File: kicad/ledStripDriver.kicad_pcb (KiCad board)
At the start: 2 copper layers, 110 x 91 mm, 50 parts, among them J1 AudioJack3_SwitchTR, K1 G5RL1AELN5DC, Q1 Q_NPN_BEC_S8050, Q2 AO3400, Q3 AO3400, Q4 AO3400, SW1 SW_DIP_x01, SW2 Rotary_Encoder_Switch, SW3 SW_Push, U1 MOD_ESP32_DEV_universal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

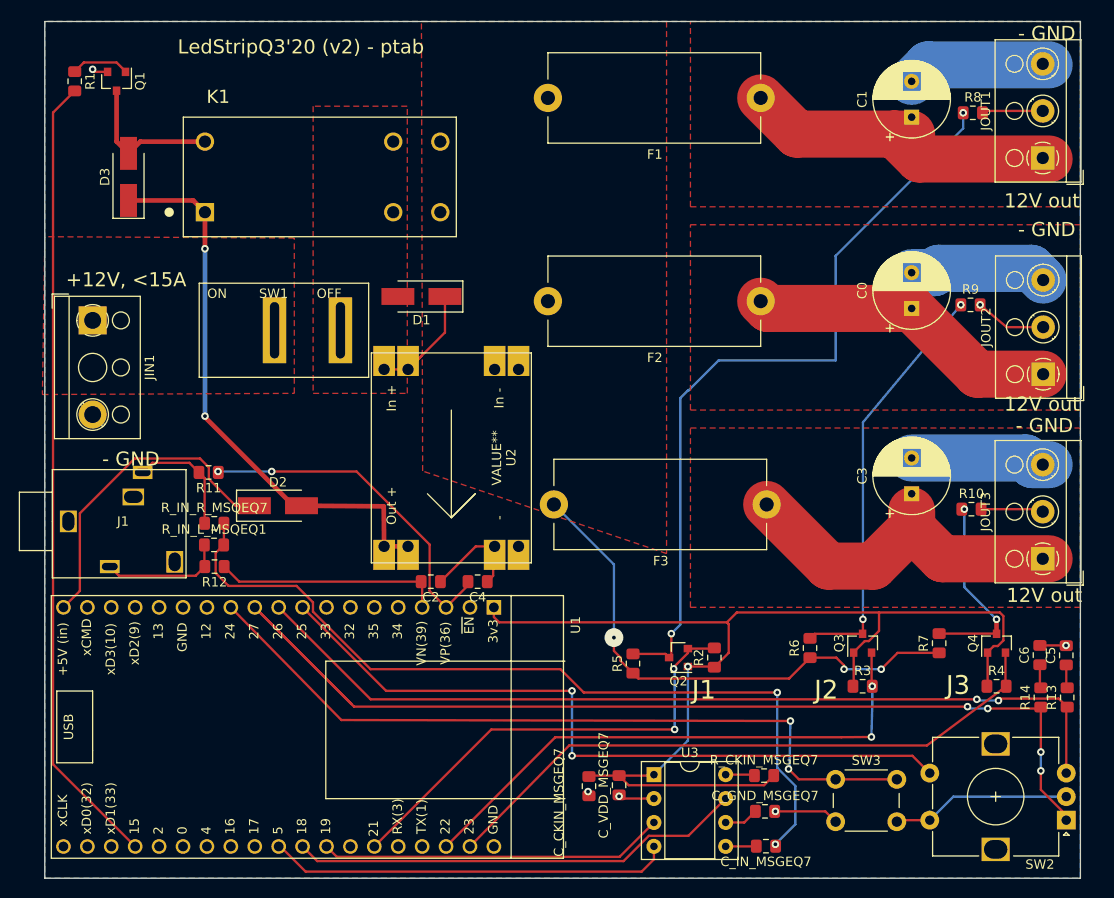
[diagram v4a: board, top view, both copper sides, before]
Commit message: PCB v3: Hopefully manufacturing ready.
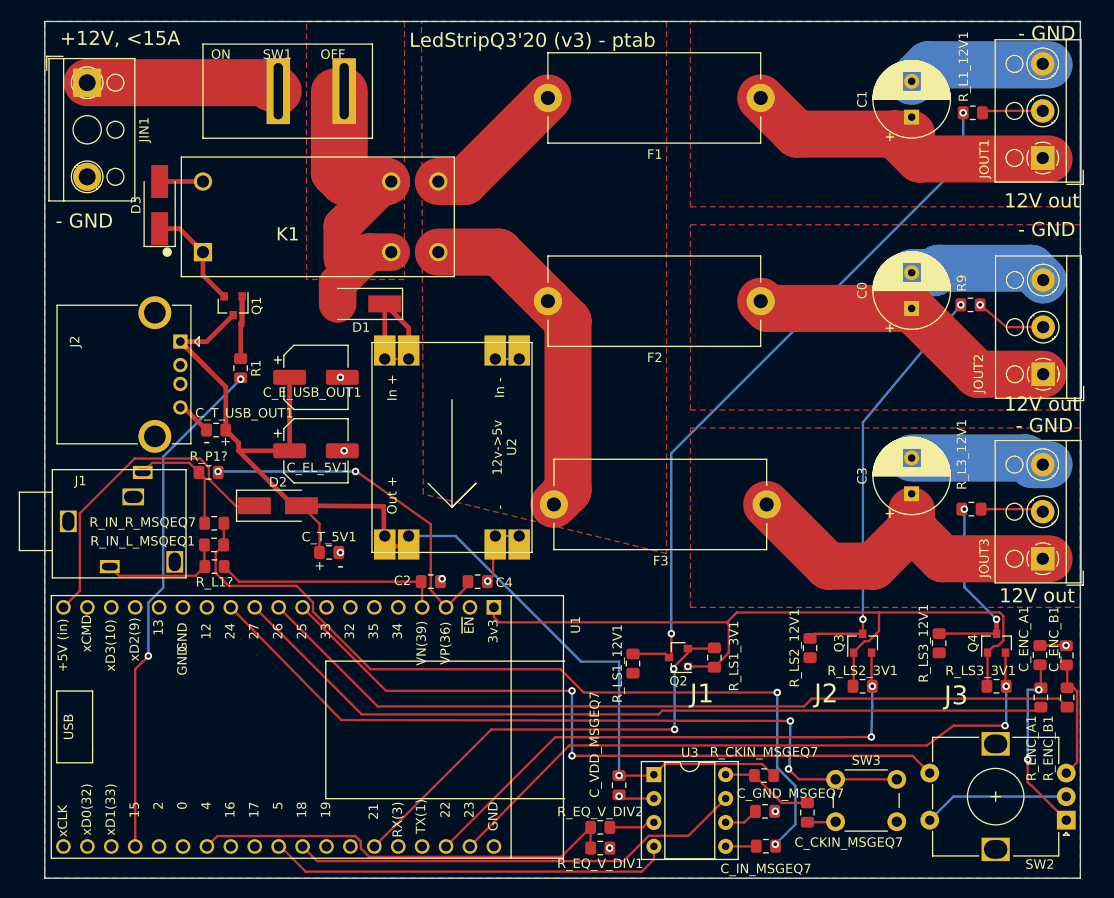
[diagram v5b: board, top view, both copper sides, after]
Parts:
- added C_EL_5V1: >50uF, Capacitor_SMD:CP_Elec_6.3x5.4, F.Cu at (128.8, 95.6)
- added C_E_USB_OUT1: >20uF, Capacitor_SMD:CP_Elec_6.3x5.4, F.Cu at (128.8, 87.8)
- added C_T_5V1: 1uF, Capacitor_SMD:C_0805_2012Metric_Pad1.15x1.40mm_HandSolder, F.Cu at (130.2, 106.4)
- added C_T_USB_OUT1: >1uF, Capacitor_SMD:C_0805_2012Metric_Pad1.15x1.40mm_HandSolder, F.Cu at (118.2, 93.4)
- added J2: USB_POWER_OUT, Connector_USB:USB_A_CONNFLY_DS1095-WNR0, F.Cu at (114.4, 84.0)
- added R_EQ_V_DIV1: 10k, Resistor_SMD:R_0805_2012Metric_Pad1.15x1.40mm_HandSolder, F.Cu at (159.0, 137.8)
- added R_EQ_V_DIV2: 10k, Resistor_SMD:R_0805_2012Metric_Pad1.15x1.40mm_HandSolder, F.Cu at (159.0, 135.6)
- R1: value 47ohm -> ~47ohm
- R9: value 300ohm -> R_L2_12V
- R_L1?: renamed from R12; value R -> xxk?
- R_L1_12V1: renamed from R8; value 300ohm -> 300
- R_L3_12V1: renamed from R10; value 300ohm -> 300
- R_LS1_12V1: renamed from R5; value 5kOhm -> 4k7
- R_LS1_3V1: renamed from R2; value 5kOhm -> 4k7
- R_LS2_12V1: renamed from R6; value 5kOhm -> 4k7
- R_LS2_3V1: renamed from R3; value 5kOhm -> 4k7
- R_LS3_12V1: renamed from R7; value 5kOhm -> 4k7
- R_LS3_3V1: renamed from R4; value 5kOhm -> 4k7
- R_P1?: renamed from R11; value R -> xxk?
- moved R1 35.2 mm to (120.8, 86.8)
- moved Q1 26.9 mm to (120.0, 80.2)
- moved SW1 25.4 mm to (124.8, 57.4)
- moved JIN1 25.3 mm to (104.5, 56.5)
- moved C_CKIN_MSGEQ7 23.4 mm to (181.0, 134.0)
- moved D1 6.45 mm to (133.6, 80.0)
- moved D3 4.46 mm to (112.2, 69.5)
- moved K1 4.25 mm to (129.0, 70.8)
- moved U2 1.11 mm to (143.2, 95.2)
- renumbered C6 to C_ENC_A1, C5 to C_ENC_B1, R14 to R_ENC_A1, R13 to R_ENC_B1
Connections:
- C_CKIN_MSGEQ7 pad 1: +3V3 -> Net-(C_CKIN_MSGEQ7-Pad1)
- C_ENC_A1 pad 1: Net-(C6-Pad1) -> Net-(C_ENC_A1-Pad1)
- C_ENC_B1 pad 1: Net-(C5-Pad1) -> Net-(C_ENC_B1-Pad1)
- C_VDD_MSGEQ7 pad 2: +3V3 -> +5V
- D3 pad 1: +5V -> Net-(D3-Pad1)
- D3 pad 2: Net-(D3-Pad2) -> GND
- J1 pad RN: Net-(J1-PadRN) -> (no net)
- J1 pad TN: Net-(J1-PadTN) -> (no net)
- K1 pad 1: +5V -> Net-(D3-Pad1)
- K1 pad 8: Net-(D3-Pad2) -> GND
- Q1 pad 2: GND -> Net-(D3-Pad1)
- Q1 pad 3: Net-(D3-Pad2) -> +5V
- R_CKIN_MSGEQ7 pad 1: Net-(R_CKIN_MSGEQ7-Pad1) -> Net-(C_CKIN_MSGEQ7-Pad1)
- R_CKIN_MSGEQ7 pad 2: +3V3 -> +5V
- R_ENC_A1 pad 1: Net-(R14-Pad1) -> Net-(R_ENC_A1-Pad1)
- R_ENC_A1 pad 2: Net-(C6-Pad1) -> Net-(C_ENC_A1-Pad1)
- R_ENC_B1 pad 1: Net-(R13-Pad1) -> Net-(R_ENC_B1-Pad1)
- R_ENC_B1 pad 2: Net-(C5-Pad1) -> Net-(C_ENC_B1-Pad1)
- R_LS1_12V1 pad 1: /12V_POST_RELAY -> (no net)
- R_LS2_12V1 pad 1: /12V_POST_RELAY -> (no net)
- R_LS3_12V1 pad 1: /12V_POST_RELAY -> (no net)
- SW2 pad A: Net-(R14-Pad1) -> Net-(C_ENC_A1-Pad1)
- SW2 pad B: Net-(R13-Pad1) -> Net-(C_ENC_B1-Pad1)
- U1 pad 10: Net-(R13-Pad1) -> Net-(R_ENC_B1-Pad1)
- U1 pad 11: Net-(R14-Pad1) -> Net-(R_ENC_A1-Pad1)
- U1 pad 13: Net-(U1-Pad13) -> (no net)
- U1 pad 14: GND -> (no net)
- U1 pad 15: Net-(U1-Pad15) -> (no net)
- U1 pad 16: Net-(U1-Pad16) -> (no net)
- U1 pad 17: Net-(U1-Pad17) -> (no net)
- U1 pad 18: Net-(U1-Pad18) -> (no net)
- U1 pad 2: Net-(U1-Pad2) -> (no net)
- U1 pad 20: Net-(U1-Pad20) -> (no net)
- U1 pad 23: Net-(U1-Pad23) -> (no net)
- U1 pad 24: Net-(U1-Pad24) -> (no net)
- U1 pad 26: Net-(U1-Pad26) -> (no net)
- U1 pad 27: Net-(U1-Pad27) -> (no net)
- U1 pad 30: Net-(U1-Pad30) -> (no net)
- U1 pad 31: Net-(U1-Pad31) -> (no net)
- U1 pad 33: Net-(U1-Pad33) -> (no net)
- U1 pad 34: Net-(U1-Pad34) -> (no net)
- U1 pad 36: Net-(U1-Pad36) -> (no net)
- U1 pad 37: Net-(U1-Pad37) -> (no net)
- U1 pad 38: Net-(U1-Pad38) -> (no net)
- U1 pad 40: Net-(U1-Pad40) -> (no net)
- U1 pad 41: Net-(U1-Pad41) -> (no net)
- U1 pad 5: Net-(U1-Pad5) -> (no net)
- U1 pad 6: Net-(U1-Pad6) -> (no net)
- U1 pad 7: Net-(U1-Pad7) -> (no net)
- U1 pad 8: Net-(U1-Pad8) -> (no net)
- U3 pad 1: +3V3 -> +5V
- U3 pad 3: Net-(U1-Pad27) -> Net-(R_EQ_V_DIV2-Pad2)
- U3 pad 8: Net-(R_CKIN_MSGEQ7-Pad1) -> Net-(C_CKIN_MSGEQ7-Pad1)
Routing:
- net Net-(R14-Pad1): track 115.7 -> 0.00 mm, vias 4 -> 0
- net Net-(R13-Pad1): track 95.4 -> 0.00 mm, vias 2 -> 0
- net Net-(R_ENC_B1-Pad1): track 0.00 -> 88.8 mm
- net Net-(R_ENC_A1-Pad1): track 0.00 -> 88.5 mm
- net +5V: track 60.1 -> 126.2 mm, vias 2 -> 1
- net /12V_PRE_RELAY: track 0.00 -> 47.3 mm
- net Net-(R_EQ_V_DIV1-Pad2): track 0.00 -> 46.1 mm
- net +12V: track 0.00 -> 40.3 mm
- net +3V3: track 119.2 -> 82.0 mm
- net Net-(U1-Pad27): track 36.8 -> 0.00 mm
- net /RELAY_DRIVER: track 84.8 -> 54.3 mm, vias 0 -> 2
- net Net-(C_ENC_A1-Pad1): track 0.00 -> 19.7 mm, vias 0 -> 2
- net Net-(D3-Pad2): track 15.8 -> 0.00 mm
- net Net-(C_ENC_B1-Pad1): track 0.00 -> 13.0 mm
- net Net-(D3-Pad1): track 0.00 -> 11.3 mm
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- removed copper zone on F.Cu, net +12V
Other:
- board text added: "+"
- board text added: "-"
- board text added: "LedStripQ3'20 (v3) - ptab"
- board text removed: "LedStripQ3'20 (v2) - ptab"

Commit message: With charging port.
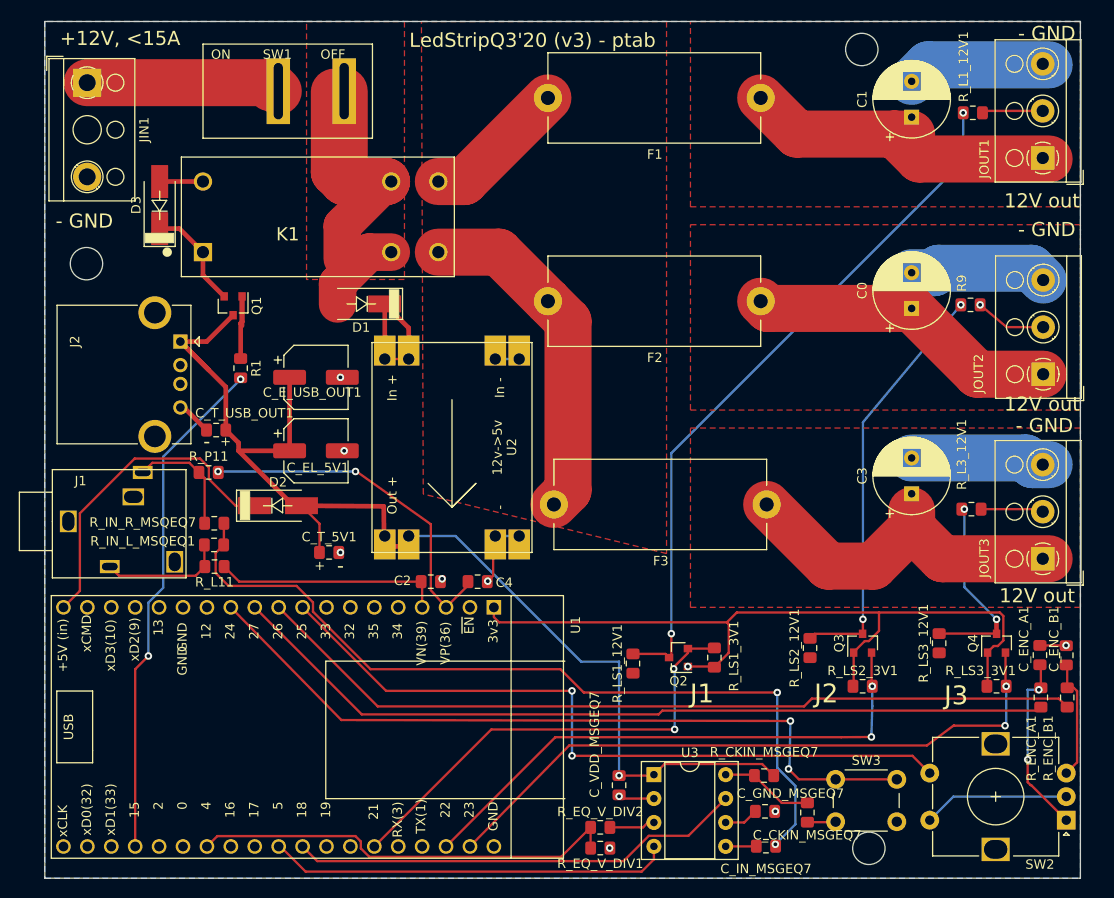
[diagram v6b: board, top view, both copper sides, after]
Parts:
- D1, D2, D3: footprint Diode_SMD:D_SMA_Handsoldering -> ptabOther:D_SMA_Handsoldering
- gave numbers to parts that had none: 2
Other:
- outline, holes or cut-outs redrawn

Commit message: v3 - working and split between files. StroboRainbows.
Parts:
- moved D3 5.94 mm to (109.0, 74.5)
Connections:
- R_LS1_12V1 pad 1: (no net) -> /12V_POST_RELAY
- R_LS2_12V1 pad 1: (no net) -> /12V_POST_RELAY
- R_LS3_12V1 pad 1: (no net) -> /12V_POST_RELAY
- U1 pad 14: (no net) -> Net-(U1-Pad14)
- U1 pad 20: (no net) -> Net-(U1-Pad14)
- U1 pad 26: (no net) -> Net-(U1-Pad14)
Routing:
- net /12V_POST_RELAY: track 52.2 -> 109.8 mm, vias 0 -> 4
- net Net-(U1-Pad14): track 0.00 -> 48.9 mm
- net GND: track 88.8 -> 94.1 mm
- net Net-(D3-Pad1): track 11.3 -> 14.5 mm
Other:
- board text added: "LedStripQ4'20 (v4) - ptab"
- board text removed: "LedStripQ3'20 (v3) - ptab"

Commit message: v4 - preprod
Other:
- board text added: "LedStripQ1'21 (v4) - ptab"
- board text removed: "LedStripQ4'20 (v4) - ptab"
